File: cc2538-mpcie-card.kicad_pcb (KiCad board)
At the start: 2 copper layers, 30.1 x 50.8 mm, 27 parts, among them J1 Bus_PCI_Express_Mini, J2 Conn_ARM_JTAG_SWD_10, Q1 MUN5214DW1, Q2 MUN5214DW1, U1 CC2538_SZ12, U2 CP2102N-A01-GQFN24

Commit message: Increased GND plane clearance to 0.35mm
The current GND plane is too near the edge in the prototype boards.
Increased the clearance because it is unnecessary to have such a tight
clearance for the GND plane anyway.
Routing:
- net GND: vias 49 -> 52
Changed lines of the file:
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@@
     (thickness 1.6)
     (drawings 48)
-    (tracks 319)
+    (tracks 322)
     (zones 0)
     (modules 27)
@@
     (user_trace_width 0.5)
     (trace_clearance 0.13)
-    (zone_clearance 0.2)
+    (zone_clearance 0.35)
     (zone_45_only yes)
     (trace_min 0.2)
@@
   (via (at 132.7 118.2) (size 0.6) (drill 0.3) (layers F.Cu B.Cu) (net 1))
   (via (at 132.4 123.2) (size 0.6) (drill 0.3) (layers F.Cu B.Cu) (net 1))
+  (via (at 149.5 140.65) (size 0.6) (drill 0.3) (layers F.Cu B.Cu) (net 1))
+  (via (at 146.2 136.2) (size 0.6) (drill 0.3) (layers F.Cu B.Cu) (net 1))
+  (via (at 145.05 140.65) (size 0.6) (drill 0.3) (layers F.Cu B.Cu) (net 1))
   (segment (start 149.3 150.4) (end 149.3 148.35) (width 0.2) (layer B.Cu) (net 2) (status 10))
   (segment (start 149.3 148.35) (end 148.8 147.85) (width 0.2) (layer B.Cu) (net 2))
@@
   )
   (zone (net 1) (net_name GND) (layer F.Cu) (hatch edge 0.508)
-    (connect_pads (clearance 0.2))
+    (connect_pads (clearance 0.35))
     (min_thickness 0.2)
     (fill yes (arc_segments 32) (thermal_gap 0.2) (thermal_bridge_width 0.508) (smoothing fillet) (radius 0.3))
@@
   )
   (zone (net 1) (net_name GND) (layer B.Cu) (hatch edge 0.508)
-    (connect_pads (clearance 0.2))
+    (connect_pads (clearance 0.35))
     (min_thickness 0.2)
     (fill yes (arc_segments 32) (thermal_gap 0.2) (thermal_bridge_width 0.508) (smoothing fillet) (radius 0.3))

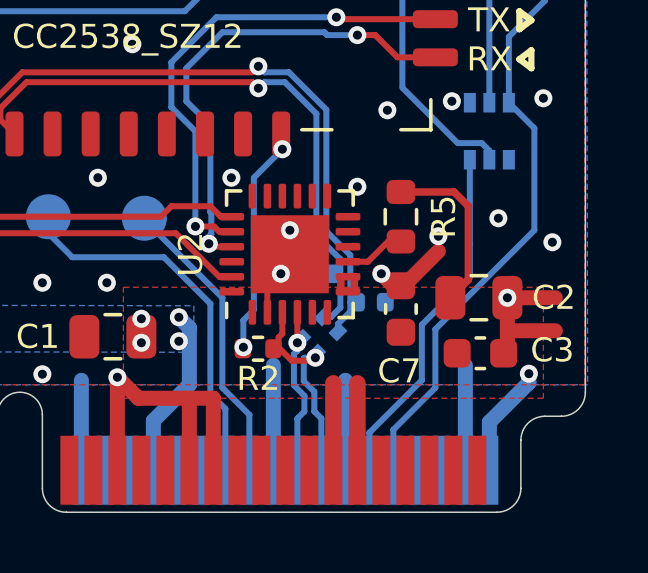
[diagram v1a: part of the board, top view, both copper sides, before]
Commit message: Reduce thermal spokes to 0.3mm
Found it difficult to solder the GND pins of the Zigbee module. I'm not
sure if the heat was being conducted away by the GND plane on the
castellated GND pads of the module, or by the GND plane on this board.

In either case, it's safer to just reduce the spoke widths of the copper
pours, since 0.508mm for thermal spokes is an overkill anyway. In
addition, thermal clearance is also increased to pull the pours away
from the pad, hopefully reducing thermal conduction.
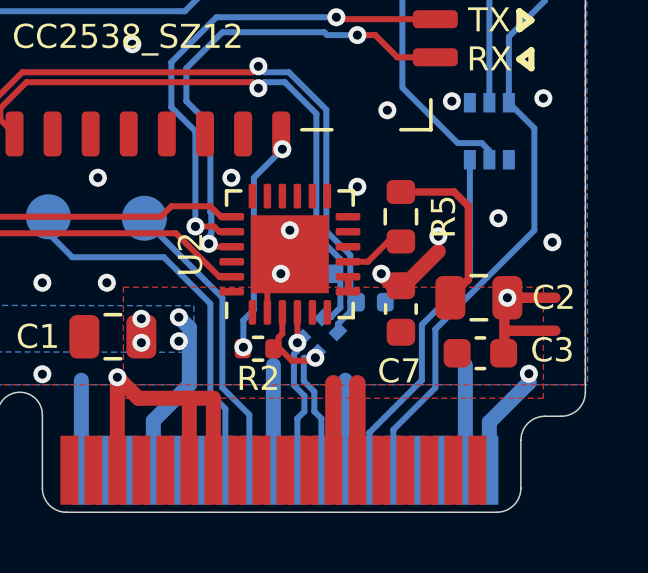
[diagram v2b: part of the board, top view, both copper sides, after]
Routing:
- net +3V3: track 78.8 -> 78.3 mm
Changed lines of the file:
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@@
     (user_trace_width 0.5)
     (trace_clearance 0.13)
-    (zone_clearance 0.35)
+    (zone_clearance 0.3)
     (zone_45_only yes)
     (trace_min 0.2)
@@
   (segment (start 145.7 147.3) (end 145.7 147.3) (width 0.5) (layer F.Cu) (net 1))
   (segment (start 158.7 146.375) (end 158.575 146.5) (width 0.5) (layer F.Cu) (net 1))
-  (segment (start 158.7 144.65) (end 160.3 144.65) (width 0.5) (layer F.Cu) (net 1))
-  (segment (start 158.7 144.65) (end 158.7 146.375) (width 0.5) (layer F.Cu) (net 1))
-  (segment (start 158.7 145.75) (end 160.3 145.75) (width 0.5) (layer F.Cu) (net 1))
+  (segment (start 158.7 144.65) (end 160.3 144.65) (width 0.35) (layer F.Cu) (net 1))
+  (segment (start 158.6 144.65) (end 158.6 146.375) (width 0.35) (layer F.Cu) (net 1))
   (via (at 143.6 122.6) (size 0.6) (drill 0.3) (layers F.Cu B.Cu) (net 1))
   (via (at 146.8 122.75) (size 0.6) (drill 0.3) (layers F.Cu B.Cu) (net 1))
@@
   (via (at 146.2 136.2) (size 0.6) (drill 0.3) (layers F.Cu B.Cu) (net 1))
   (via (at 145.05 140.65) (size 0.6) (drill 0.3) (layers F.Cu B.Cu) (net 1))
+  (segment (start 158.7 145.75) (end 160.3 145.75) (width 0.35) (layer F.Cu) (net 1))
+  (segment (start 160.3 145.75) (end 160.3 145.75) (width 0.35) (layer F.Cu) (net 1))
   (segment (start 149.3 150.4) (end 149.3 148.35) (width 0.2) (layer B.Cu) (net 2) (status 10))
   (segment (start 149.3 148.35) (end 148.8 147.85) (width 0.2) (layer B.Cu) (net 2))
@@
   (segment (start 133.6 141.8) (end 134.15 142.35) (width 0.2) (layer F.Cu) (net 8))
   (via (at 134.15 142.35) (size 0.6) (drill 0.3) (layers F.Cu B.Cu) (net 8))
-  (segment (start 153.15 143.95) (end 153.15 144.45) (width 0.25) (layer F.Cu) (net 8) (status 30))
-  (segment (start 153.6 143.95) (end 153.6 144.45) (width 0.25) (layer F.Cu) (net 8) (status 30))
   (segment (start 134.15 142.35) (end 134.15 142.35) (width 0.2) (layer F.Cu) (net 8))
+  (segment (start 153.4 143.95) (end 153.4 144.45) (width 0.25) (layer F.Cu) (net 8) (status 30))
   (segment (start 156.3 123.935) (end 157.565 123.935) (width 0.2) (layer F.Cu) (net 9) (status 10))
   (segment (start 157.565 123.935) (end 158.25 123.25) (width 0.2) (layer F.Cu) (net 9))
@@
   )
   (zone (net 1) (net_name GND) (layer F.Cu) (hatch edge 0.508)
-    (connect_pads (clearance 0.35))
-    (min_thickness 0.2)
-    (fill yes (arc_segments 32) (thermal_gap 0.2) (thermal_bridge_width 0.508) (smoothing fillet) (radius 0.3))
+    (connect_pads (clearance 0.3))
+    (min_thickness 0.15)
+    (fill yes (arc_segments 32) (thermal_gap 0.3) (thermal_bridge_width 0.3) (smoothing fillet) (radius 0.3))
     (polygon
       (pts
@@
   )
   (zone (net 1) (net_name GND) (layer B.Cu) (hatch edge 0.508)
-    (connect_pads (clearance 0.35))
+    (connect_pads (clearance 0.3))
     (min_thickness 0.2)
-    (fill yes (arc_segments 32) (thermal_gap 0.2) (thermal_bridge_width 0.508) (smoothing fillet) (radius 0.3))
+    (fill yes (arc_segments 32) (thermal_gap 0.3) (thermal_bridge_width 0.3) (smoothing fillet) (radius 0.3))
     (polygon
       (pts
@@
   (zone (net 8) (net_name +3V3) (layer F.Cu) (hatch edge 0.508)
     (priority 1)
-    (connect_pads (clearance 0.2))
+    (connect_pads (clearance 0.24))
     (min_thickness 0.2)
-    (fill yes (arc_segments 32) (thermal_gap 0.2) (thermal_bridge_width 0.508) (smoothing fillet) (radius 0.3))
+    (fill yes (arc_segments 32) (thermal_gap 0.2) (thermal_bridge_width 0.3) (smoothing fillet) (radius 0.3))
     (polygon
       (pts

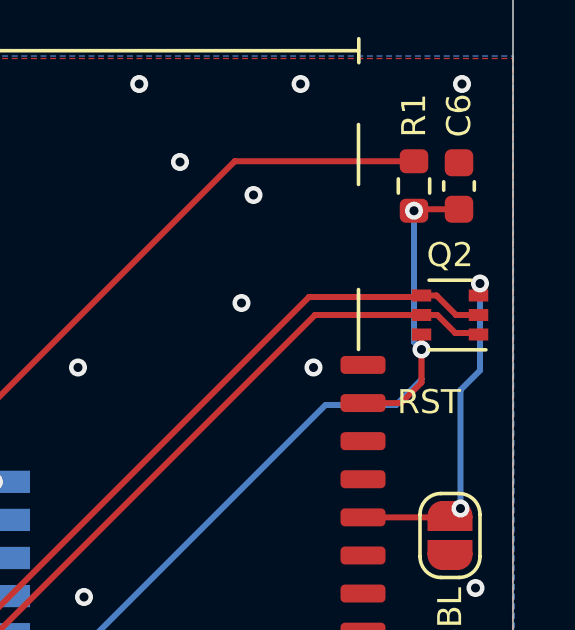
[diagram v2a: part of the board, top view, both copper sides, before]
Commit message: Added Q2 bridge silkscreen & some schematic text
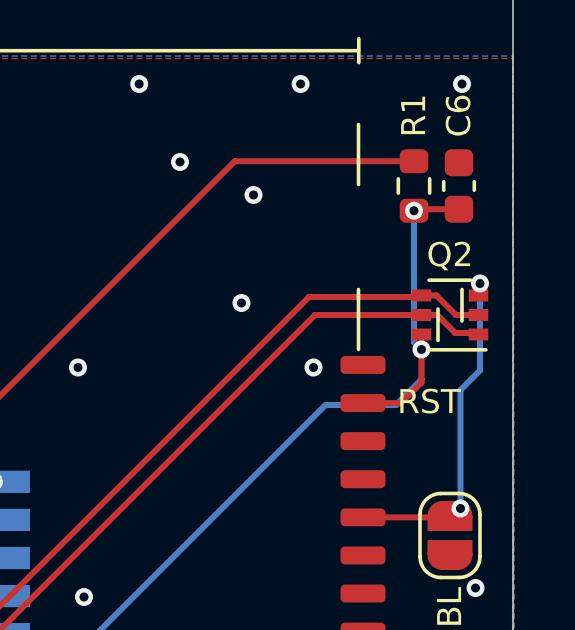
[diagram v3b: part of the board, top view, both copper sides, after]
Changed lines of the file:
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@@
   (general
     (thickness 1.6)
-    (drawings 48)
+    (drawings 50)
     (tracks 322)
     (zones 0)
@@
     )
   )
+  (gr_line (start 158.8 120.8) (end 158.8 121.85) (layer F.SilkS) (width 0.12))
+  (gr_line (start 159.6 120.15) (end 159.6 121.2) (layer F.SilkS) (width 0.12))
   (gr_line (start 159.5 137) (end 159.1 136.7) (layer F.SilkS) (width 0.21))
   (gr_line (start 159.5 137) (end 159.5 136.4) (layer F.SilkS) (width 0.21))

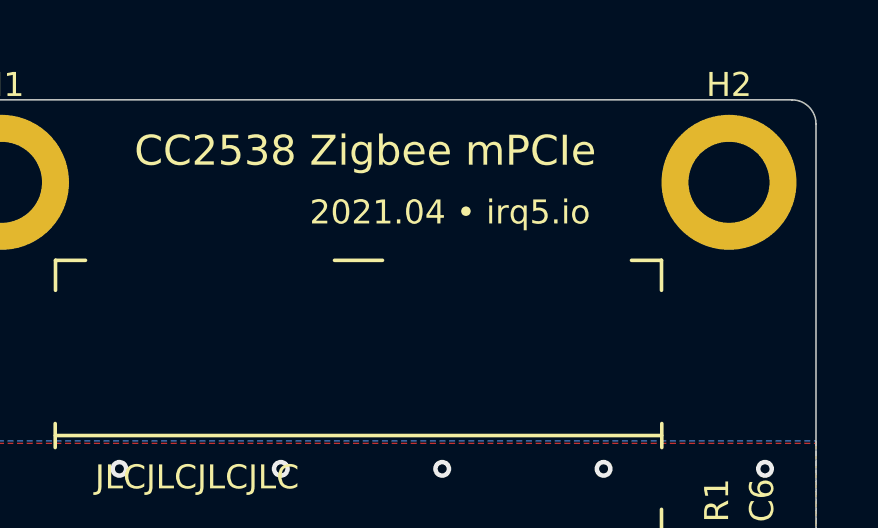
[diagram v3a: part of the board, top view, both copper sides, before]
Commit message: Updated PCB, bumped revision numbers
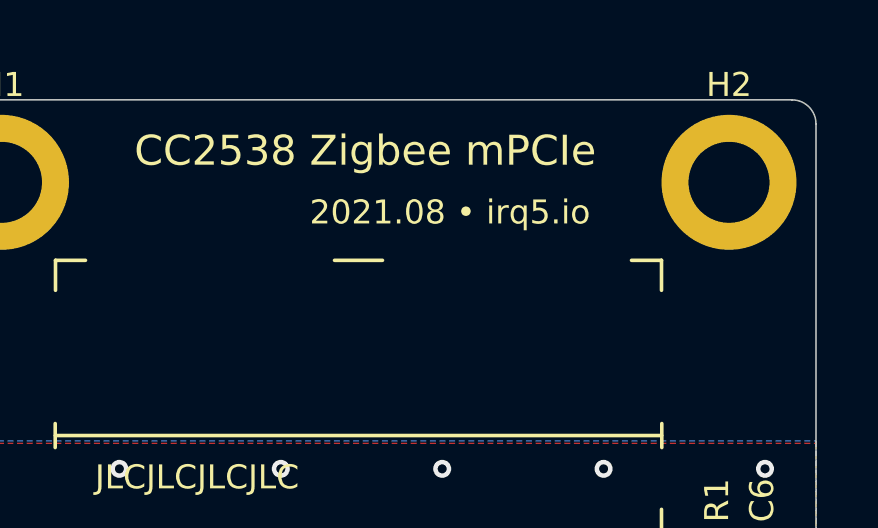
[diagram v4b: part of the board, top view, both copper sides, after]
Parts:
- R3: value 200R -> 4K7
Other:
- board text added: "2021.08 • irq5.io"
- board text removed: "2021.04 • irq5.io"
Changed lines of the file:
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@@
   (title_block
     (title "CC2538 Zigbee mPCIe")
-    (rev 2021.04)
+    (rev 2021.08)
   )
   (layers
@@
       (effects (font (size 0.8 0.8) (thickness 0.1)))
     )
-    (fp_text value 200R (at 0 1.43 90) (layer F.Fab)
+    (fp_text value 4K7 (at 0 1.43 90) (layer F.Fab)
       (effects (font (size 1 1) (thickness 0.15)))
     )
@@
     (effects (font (size 0.8 0.8) (thickness 0.1)) (justify right mirror))
   )
-  (gr_text "2021.04 • irq5.io" (at 149.1 104.75) (layer F.SilkS)
+  (gr_text "2021.08 • irq5.io" (at 149.1 104.75) (layer F.SilkS)
     (effects (font (size 0.8 0.8) (thickness 0.1)))
   )
